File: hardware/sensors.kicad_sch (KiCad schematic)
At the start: 2 parts

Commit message: train schematics
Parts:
- added C? (x5): 0.1u, Capacitor_SMD:C_0603_1608Metric, symbol Device:C_Small
- added C? (x2): 4.7u, Capacitor_SMD:C_0805_2012Metric, symbol Device:C_Small
- added R? (x4): 4.7k, Resistor_SMD:R_0603_1608Metric, symbol Device:R_Small
- added R? (x5): 10k, Resistor_SMD:R_0603_1608Metric, symbol Device:R_Small
- U?: footprint (none) -> bt_Package_LGA:TE_MS563702BA03-50
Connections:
- net VDD_AUX_3V3: now reaches U?. (VDD)
- net VDD_AUX_3V3: now also U?.14 (VDD), C?.1, C?.1, C?.1, C?.1, R?.1, R?.1, R?.1, R?.1, R?.1, R?.1
- net at U?.1 (VDDIO): now also C?.1
- net at U?.10 (SA1/CS_B): now also R?.1, R?.2
- net IMU_INT1: now reaches U?.11 (INT1)
- net IMU_INT1: now also R?.2
- net GND: now reaches U?.12 (GND)
- net GND: now also U?.13 (RSVD), U?.3 (RSVD), U?.5 (GND), C?.2, C?.2, C?.2, C?.2, C?.2, R?.2, R?.2, R?.2
- net at U?.16 (RST): now also R?.1
- net at U?.2 (BYP): now also C?.1
- net SENSOR_I2C.SCL: now reaches U?.4 (SCL/SCLK)
- net SENSOR_I2C.SCL: now also U?. (VDD), R?.2
- net SENSOR_I2C.SDA: now reaches U?.6 (SDA/MOSI)
- net SENSOR_I2C.SDA: now also U?. (VDD), R?.2
- net at U?.7 (SA0/MISO): now also R?.1, R?.2
- net at U?.8 (CRST): now also C?.1
- net IMU_INT2: now reaches U?.9 (INT2)
- net IMU_INT2: now also R?.2
- new net: C?.2, C?.2, U?. (VDD)
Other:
- note added: "0xEC/0xED"
- note added: "SA1 SA0 I2C R/W ------------- 1 0 0x38/0x39 0 1 0x3A/0x3B 0 0 0x3C/0x3D 1 1 0x3E/0x3F"
- company: Erdapfel -> Frisius
- moved on the sheet: U?

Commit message: started b2b and power
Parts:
- removed R?: 4.7k, Resistor_SMD:R_0603_1608Metric, symbol Device:R_Small
- added TP?: IMU_ALERT, symbol Connector:TestPoint
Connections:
- net IMU_INT1: no longer names the net of R?.2, U?.11 (INT1)
- net IMU_INT1: now also TP?.1
- net IMU_INT2: no longer names the net of U?.9 (INT2)
- no-connect marks 0 -> 1
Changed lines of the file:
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@@
   (junction (at 43.18 82.55) (diameter 0) (color 0 0 0 0)
   )
-  (junction (at 119.38 27.94) (diameter 0) (color 0 0 0 0)
-  )
-  (junction (at 124.46 45.72) (diameter 0) (color 0 0 0 0)
+  (junction (at 119.38 41.91) (diameter 0) (color 0 0 0 0)
   )
   (junction (at 137.16 77.47) (diameter 0) (color 0 0 0 0)
@@
   (junction (at 78.74 36.83) (diameter 0) (color 0 0 0 0)
   )
-  (junction (at 119.38 43.18) (diameter 0) (color 0 0 0 0)
-  )
   (junction (at 114.3 27.94) (diameter 0) (color 0 0 0 0)
   )
@@
   (junction (at 43.18 36.83) (diameter 0) (color 0 0 0 0)
   )
+  (no_connect (at 96.52 76.2))
   (bus_entry (at 148.59 36.83) (size -2.54 2.54)
     (stroke (width 0) (type default) (color 0 0 0 0))
@@
     (stroke (width 0) (type default) (color 0 0 0 0))
   )
-  (wire (pts (xy 119.38 27.94) (xy 124.46 27.94))
-    (stroke (width 0) (type default) (color 0 0 0 0))
-  )
   (wire (pts (xy 134.62 76.2) (xy 134.62 77.47))
     (stroke (width 0) (type default) (color 0 0 0 0))
@@
     (stroke (width 0) (type default) (color 0 0 0 0))
   )
-  (wire (pts (xy 124.46 45.72) (xy 151.13 45.72))
-    (stroke (width 0) (type default) (color 0 0 0 0))
-  )
   (wire (pts (xy 109.22 26.67) (xy 109.22 27.94))
     (stroke (width 0) (type default) (color 0 0 0 0))
@@
     (stroke (width 0) (type default) (color 0 0 0 0))
   )
-  (wire (pts (xy 119.38 73.66) (xy 119.38 43.18))
+  (wire (pts (xy 119.38 34.29) (xy 119.38 41.91))
     (stroke (width 0) (type default) (color 0 0 0 0))
   )
@@
     (stroke (width 0) (type default) (color 0 0 0 0))
   )
-  (wire (pts (xy 119.38 43.18) (xy 151.13 43.18))
-    (stroke (width 0) (type default) (color 0 0 0 0))
-  )
   (bus (pts (xy 149.86 31.75) (xy 148.59 33.02))
     (stroke (width 0) (type default) (color 0 0 0 0))
@@
     (stroke (width 0) (type default) (color 0 0 0 0))
   )
-  (wire (pts (xy 119.38 34.29) (xy 119.38 43.18))
-    (stroke (width 0) (type default) (color 0 0 0 0))
-  )
   (wire (pts (xy 68.58 44.45) (xy 78.74 44.45))
     (stroke (width 0) (type default) (color 0 0 0 0))
@@
     (stroke (width 0) (type default) (color 0 0 0 0))
   )
-  (wire (pts (xy 96.52 76.2) (xy 124.46 76.2))
-    (stroke (width 0) (type default) (color 0 0 0 0))
-  )
   (wire (pts (xy 50.8 82.55) (xy 58.42 82.55))
     (stroke (width 0) (type default) (color 0 0 0 0))
   )
-  (wire (pts (xy 124.46 27.94) (xy 124.46 29.21))
-    (stroke (width 0) (type default) (color 0 0 0 0))
-  )
   (wire (pts (xy 58.42 64.77) (xy 58.42 69.85))
     (stroke (width 0) (type default) (color 0 0 0 0))
@@
     (stroke (width 0) (type default) (color 0 0 0 0))
   )
-  (wire (pts (xy 124.46 76.2) (xy 124.46 45.72))
-    (stroke (width 0) (type default) (color 0 0 0 0))
-  )
   (wire (pts (xy 96.52 82.55) (xy 97.79 82.55))
     (stroke (width 0) (type default) (color 0 0 0 0))
@@
     (stroke (width 0) (type default) (color 0 0 0 0))
   )
-  (wire (pts (xy 124.46 34.29) (xy 124.46 45.72))
+  (wire (pts (xy 119.38 41.91) (xy 119.38 73.66))
     (stroke (width 0) (type default) (color 0 0 0 0))
   )
@@
   )
   (hierarchical_label "SENSOR_I2C{SDA SCL}" (shape bidirectional) (at 151.13 31.75 0)
-    (effects (font (size 0.8 0.8)) (justify left))
-  )
-  (hierarchical_label "IMU_INT2" (shape bidirectional) (at 151.13 45.72 0)
-    (effects (font (size 0.8 0.8)) (justify left))
-  )
-  (hierarchical_label "IMU_INT1" (shape bidirectional) (at 151.13 43.18 0)
     (effects (font (size 0.8 0.8)) (justify left))
   )
@@
     (pin "1")
     (pin "2")
+  )
+  (symbol (lib_id "Connector:TestPoint") (at 119.38 41.91 270) (unit 1)
+    (in_bom yes) (on_board yes)
+    (property "Reference" "TP?" (id 0) (at 123.825 41.91 90)
+      (effects (font (size 0.8 0.8)) (justify left))
+    )
+    (property "Value" "IMU_ALERT" (id 1) (at 121.92 44.45 0)
+      (effects (font (size 0.8 0.8)) (justify left) hide)
+    )
+    (property "Footprint" "" (id 2) (at 119.38 46.99 0)
+      (effects (font (size 1.27 1.27)) hide)
+    )
+    (property "Datasheet" "~" (id 3) (at 119.38 46.99 0)
+      (effects (font (size 1.27 1.27)) hide)
+    )
+    (pin "1")
   )
   (symbol (lib_id "Device:R_Small") (at 119.38 31.75 0) (unit 1)
@@
     (pin "1")
   )
-  (symbol (lib_id "Device:R_Small") (at 124.46 31.75 0) (unit 1)
-    (in_bom yes) (on_board yes)
-    (property "Reference" "R?" (id 0) (at 125.73 30.48 0)
-      (effects (font (size 0.8 0.8)) (justify left))
-    )
-    (property "Value" "4.7k" (id 1) (at 125.73 31.75 0)
-      (effects (font (size 0.8 0.8)) (justify left))
-    )
-    (property "Footprint" "Resistor_SMD:R_0603_1608Metric" (id 2) (at 124.46 31.75 0)
-      (effects (font (size 0.8 0.8)) hide)
-    )
-    (property "Datasheet" "~" (id 3) (at 124.46 31.75 0)
-      (effects (font (size 0.8 0.8)) hide)
-    )
-    (pin "1")
-    (pin "2")
-  )
 )

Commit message: ready for first review
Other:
- moved on the sheet: C?, R?, TP?, U?

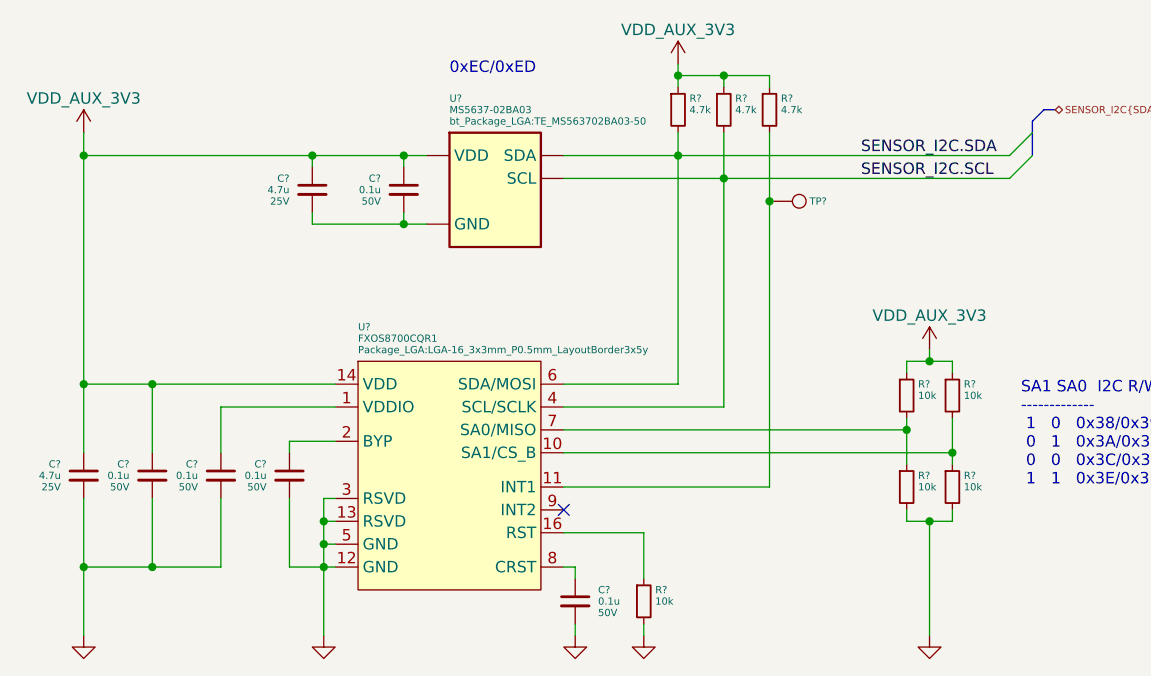
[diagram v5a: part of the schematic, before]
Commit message: checking footprint assignment, added current sense pac1934 for dev
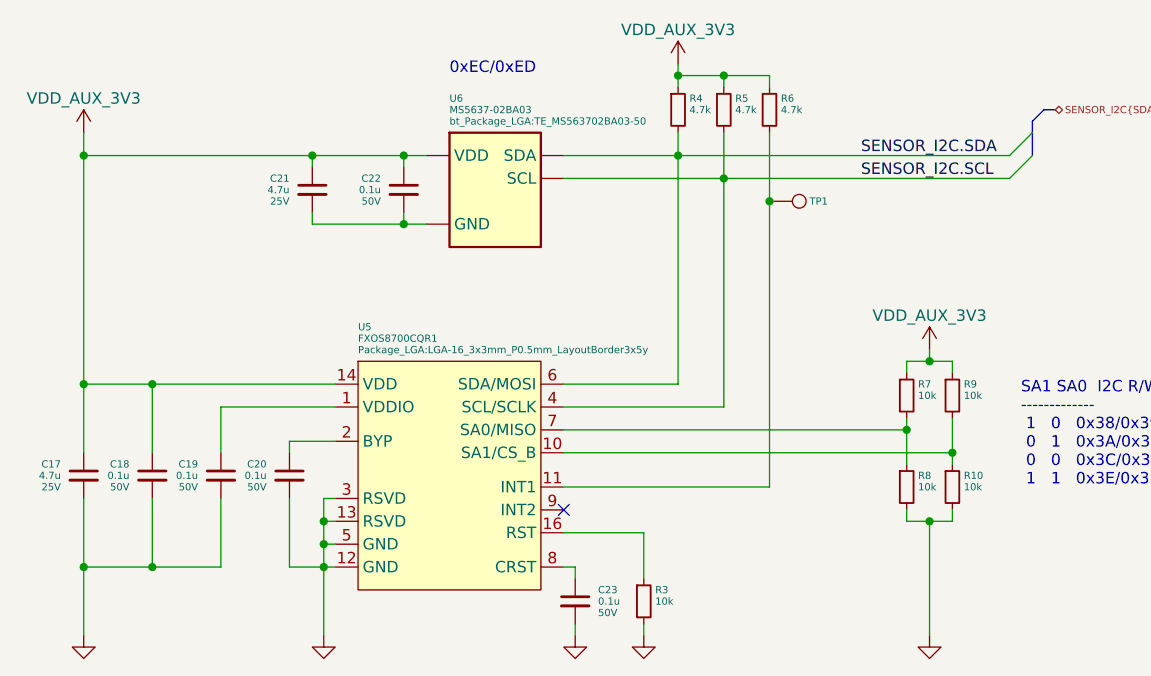
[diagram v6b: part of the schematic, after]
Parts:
- TP1: renamed from TP?; footprint (none) -> TestPoint:TestPoint_Pad_1.5x1.5mm
- gave numbers to parts that had none: 17
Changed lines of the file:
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@@
   (symbol (lib_id "Device:C_Small") (at 110.49 113.03 0) (mirror y) (unit 1)
     (in_bom yes) (on_board yes)
-    (property "Reference" "C?" (id 0) (at 107.95 111.76 0)
+    (property "Reference" "C19" (id 0) (at 107.95 111.76 0)
       (effects (font (size 0.8 0.8)) (justify left))
     )
@@
   (symbol (lib_id "Device:R_Small") (at 166.37 72.39 0) (unit 1)
     (in_bom yes) (on_board yes)
-    (property "Reference" "R?" (id 0) (at 167.64 71.12 0)
+    (property "Reference" "R5" (id 0) (at 167.64 71.12 0)
       (effects (font (size 0.8 0.8)) (justify left))
     )
@@
   (symbol (lib_id "Device:C_Small") (at 130.81 81.28 0) (mirror y) (unit 1)
     (in_bom yes) (on_board yes)
-    (property "Reference" "C?" (id 0) (at 128.27 80.01 0)
+    (property "Reference" "C22" (id 0) (at 128.27 80.01 0)
       (effects (font (size 0.8 0.8)) (justify left))
     )
@@
   (symbol (lib_id "bt_Sensor_Environmental:MS5637-02BA03") (at 140.97 80.01 0) (unit 1)
     (in_bom yes) (on_board yes)
-    (property "Reference" "U?" (id 0) (at 135.89 71.12 0)
+    (property "Reference" "U6" (id 0) (at 135.89 71.12 0)
       (effects (font (size 0.8 0.8)) (justify left))
     )
@@
   (symbol (lib_id "Device:C_Small") (at 118.11 113.03 0) (mirror y) (unit 1)
     (in_bom yes) (on_board yes)
-    (property "Reference" "C?" (id 0) (at 115.57 111.76 0)
+    (property "Reference" "C20" (id 0) (at 115.57 111.76 0)
       (effects (font (size 0.8 0.8)) (justify left))
     )
@@
   (symbol (lib_id "Device:C_Small") (at 149.86 127 0) (unit 1)
     (in_bom yes) (on_board yes)
-    (property "Reference" "C?" (id 0) (at 152.4 125.73 0)
+    (property "Reference" "C23" (id 0) (at 152.4 125.73 0)
       (effects (font (size 0.8 0.8)) (justify left))
     )
@@
   (symbol (lib_id "power:GND") (at 95.25 130.81 0) (unit 1)
     (in_bom yes) (on_board yes) (fields_autoplaced)
-    (property "Reference" "#PWR?" (id 0) (at 95.25 137.16 0)
+    (property "Reference" "#PWR016" (id 0) (at 95.25 137.16 0)
       (effects (font (size 1.27 1.27)) hide)
     )
@@
   (symbol (lib_id "Device:R_Small") (at 161.29 72.39 0) (unit 1)
     (in_bom yes) (on_board yes)
-    (property "Reference" "R?" (id 0) (at 162.56 71.12 0)
+    (property "Reference" "R4" (id 0) (at 162.56 71.12 0)
       (effects (font (size 0.8 0.8)) (justify left))
     )
@@
   (symbol (lib_id "Connector:TestPoint") (at 171.45 82.55 270) (unit 1)
     (in_bom yes) (on_board yes)
-    (property "Reference" "TP?" (id 0) (at 175.895 82.55 90)
+    (property "Reference" "TP1" (id 0) (at 175.895 82.55 90)
       (effects (font (size 0.8 0.8)) (justify left))
     )
@@
       (effects (font (size 0.8 0.8)) (justify left) hide)
     )
-    (property "Footprint" "" (id 2) (at 171.45 87.63 0)
+    (property "Footprint" "TestPoint:TestPoint_Pad_1.5x1.5mm" (id 2) (at 171.45 87.63 0)
       (effects (font (size 1.27 1.27)) hide)
     )
@@
   (symbol (lib_id "Device:R_Small") (at 171.45 72.39 0) (unit 1)
     (in_bom yes) (on_board yes)
-    (property "Reference" "R?" (id 0) (at 172.72 71.12 0)
+    (property "Reference" "R6" (id 0) (at 172.72 71.12 0)
       (effects (font (size 0.8 0.8)) (justify left))
     )
@@
   (symbol (lib_id "power:GND") (at 121.92 130.81 0) (unit 1)
     (in_bom yes) (on_board yes) (fields_autoplaced)
-    (property "Reference" "#PWR?" (id 0) (at 121.92 137.16 0)
+    (property "Reference" "#PWR017" (id 0) (at 121.92 137.16 0)
       (effects (font (size 1.27 1.27)) hide)
     )
@@
   (symbol (lib_id "bt_power:VDD_AUX_3V3") (at 189.23 99.06 0) (unit 1)
     (in_bom no) (on_board no)
-    (property "Reference" "U?" (id 0) (at 189.7634 99.06 0)
+    (property "Reference" "#U08" (id 0) (at 189.7634 99.06 0)
       (effects (font (size 1.27 1.27)) hide)
     )
@@
   (symbol (lib_id "power:GND") (at 149.86 130.81 0) (unit 1)
     (in_bom yes) (on_board yes) (fields_autoplaced)
-    (property "Reference" "#PWR?" (id 0) (at 149.86 137.16 0)
+    (property "Reference" "#PWR018" (id 0) (at 149.86 137.16 0)
       (effects (font (size 1.27 1.27)) hide)
     )
@@
   (symbol (lib_id "Device:C_Small") (at 120.65 81.28 0) (mirror y) (unit 1)
     (in_bom yes) (on_board yes)
-    (property "Reference" "C?" (id 0) (at 118.11 80.01 0)
+    (property "Reference" "C21" (id 0) (at 118.11 80.01 0)
       (effects (font (size 0.8 0.8)) (justify left))
     )
@@
   (symbol (lib_id "Device:R_Small") (at 186.69 114.3 0) (unit 1)
     (in_bom yes) (on_board yes)
-    (property "Reference" "R?" (id 0) (at 187.96 113.03 0)
+    (property "Reference" "R8" (id 0) (at 187.96 113.03 0)
       (effects (font (size 0.8 0.8)) (justify left))
     )
@@
   (symbol (lib_id "Device:R_Small") (at 191.77 104.14 0) (unit 1)
     (in_bom yes) (on_board yes)
-    (property "Reference" "R?" (id 0) (at 193.04 102.87 0)
+    (property "Reference" "R9" (id 0) (at 193.04 102.87 0)
       (effects (font (size 0.8 0.8)) (justify left))
     )
@@
   (symbol (lib_id "Device:C_Small") (at 95.25 113.03 0) (mirror y) (unit 1)
     (in_bom yes) (on_board yes)
-    (property "Reference" "C?" (id 0) (at 92.71 111.76 0)
+    (property "Reference" "C17" (id 0) (at 92.71 111.76 0)
       (effects (font (size 0.8 0.8)) (justify left))
     )
@@
   (symbol (lib_id "Device:R_Small") (at 191.77 114.3 0) (unit 1)
     (in_bom yes) (on_board yes)
-    (property "Reference" "R?" (id 0) (at 193.04 113.03 0)
+    (property "Reference" "R10" (id 0) (at 193.04 113.03 0)
       (effects (font (size 0.8 0.8)) (justify left))
     )
@@
   (symbol (lib_id "power:GND") (at 189.23 130.81 0) (unit 1)
     (in_bom yes) (on_board yes) (fields_autoplaced)
-    (property "Reference" "#PWR?" (id 0) (at 189.23 137.16 0)
+    (property "Reference" "#PWR020" (id 0) (at 189.23 137.16 0)
       (effects (font (size 1.27 1.27)) hide)
     )
@@
   (symbol (lib_id "Device:R_Small") (at 186.69 104.14 0) (unit 1)
     (in_bom yes) (on_board yes)
-    (property "Reference" "R?" (id 0) (at 187.96 102.87 0)
+    (property "Reference" "R7" (id 0) (at 187.96 102.87 0)
       (effects (font (size 0.8 0.8)) (justify left))
     )
@@
   (symbol (lib_id "bt_power:VDD_AUX_3V3") (at 95.25 74.93 0) (unit 1)
     (in_bom no) (on_board no)
-    (property "Reference" "U?" (id 0) (at 95.7834 74.93 0)
+    (property "Reference" "#U04" (id 0) (at 95.7834 74.93 0)
       (effects (font (size 1.27 1.27)) hide)
     )
@@
   (symbol (lib_id "bt_Sensor_Motion:FXOS8700CQR1") (at 135.89 113.03 0) (unit 1)
     (in_bom yes) (on_board yes)
-    (property "Reference" "U?" (id 0) (at 125.73 96.52 0)
+    (property "Reference" "U5" (id 0) (at 125.73 96.52 0)
       (effects (font (size 0.8 0.8)) (justify left))
     )
@@
   (symbol (lib_id "power:GND") (at 157.48 130.81 0) (unit 1)
     (in_bom yes) (on_board yes) (fields_autoplaced)
-    (property "Reference" "#PWR?" (id 0) (at 157.48 137.16 0)
+    (property "Reference" "#PWR019" (id 0) (at 157.48 137.16 0)
       (effects (font (size 1.27 1.27)) hide)
     )
@@
   (symbol (lib_id "Device:R_Small") (at 157.48 127 0) (unit 1)
     (in_bom yes) (on_board yes)
-    (property "Reference" "R?" (id 0) (at 158.75 125.73 0)
+    (property "Reference" "R3" (id 0) (at 158.75 125.73 0)
       (effects (font (size 0.8 0.8)) (justify left))
     )
@@
   (symbol (lib_id "Device:C_Small") (at 102.87 113.03 0) (mirror y) (unit 1)
     (in_bom yes) (on_board yes)
-    (property "Reference" "C?" (id 0) (at 100.33 111.76 0)
+    (property "Reference" "C18" (id 0) (at 100.33 111.76 0)
       (effects (font (size 0.8 0.8)) (justify left))
     )
@@
   (symbol (lib_id "bt_power:VDD_AUX_3V3") (at 161.29 67.31 0) (unit 1)
     (in_bom no) (on_board no)
-    (property "Reference" "U?" (id 0) (at 161.8234 67.31 0)
-      (effects (font (size 1.27 1.27)) hide)
-    )
+    (property "Reference" "#U07" (id 0) (at 161.8234 67.31 0)
+      (effects (font (size 1.27 1.27)) hide)
+    )

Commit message: hardware update
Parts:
- removed C21: 4.7u, Capacitor_SMD:C_0805_2012Metric, symbol Device:C_Small
- removed R10, R7, R8, R9: 10k, Resistor_SMD:R_0603_1608Metric, symbol Device:R_Small
- removed R6: 4.7k, Resistor_SMD:R_0603_1608Metric, symbol Device:R_Small
- removed TP1: IMU_ALERT, TestPoint:TestPoint_Pad_1.5x1.5mm, symbol Connector:TestPoint
- C11: renamed from C17; footprint Capacitor_SMD:C_0805_2012Metric -> Capacitor_SMD:C_0603_1608Metric
- C12: renamed from C18; footprint Capacitor_SMD:C_0603_1608Metric -> Capacitor_SMD:C_0402_1005Metric
- C13: renamed from C19; footprint Capacitor_SMD:C_0603_1608Metric -> Capacitor_SMD:C_0402_1005Metric
- C14: renamed from C20; footprint Capacitor_SMD:C_0603_1608Metric -> Capacitor_SMD:C_0402_1005Metric
- C15: renamed from C22; footprint Capacitor_SMD:C_0603_1608Metric -> Capacitor_SMD:C_0402_1005Metric
- C16: renamed from C23; footprint Capacitor_SMD:C_0603_1608Metric -> Capacitor_SMD:C_0402_1005Metric
- R2: renamed from R3; footprint Resistor_SMD:R_0603_1608Metric -> Resistor_SMD:R_0402_1005Metric
- R3: renamed from R4; footprint Resistor_SMD:R_0603_1608Metric -> Resistor_SMD:R_0402_1005Metric
- R4: renamed from R5; footprint Resistor_SMD:R_0603_1608Metric -> Resistor_SMD:R_0402_1005Metric
- renumbered U5 to U2, U6 to U3
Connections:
- net GND: now also U2.10 (SA1/CS_B), U2.7 (SA0/MISO)
- no-connect marks 1 -> 2

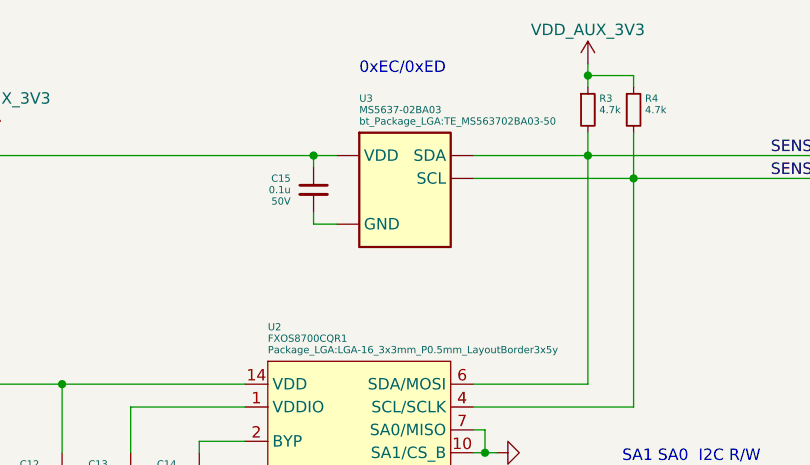
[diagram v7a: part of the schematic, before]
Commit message: initial component placement and design simplification
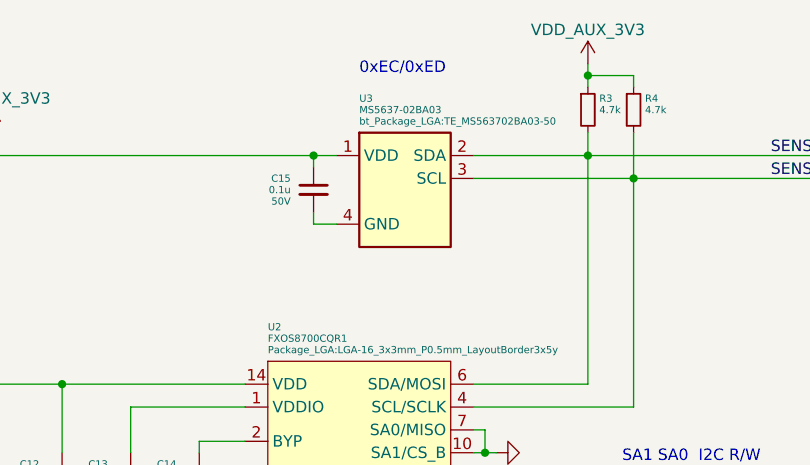
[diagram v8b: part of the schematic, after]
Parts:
- C11: footprint Capacitor_SMD:C_0603_1608Metric -> Capacitor_SMD:C_0402_1005Metric
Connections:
- net SENSOR_I2C.SCL: now also U3.3 (SCL); no longer U3. (VDD)
- net SENSOR_I2C.SDA: now also U3.2 (SDA); no longer U3. (VDD)
- net VDD_AUX_3V3: now also U3.1 (VDD); no longer U3. (VDD)
- net at C15.2: now also U3.4 (GND); no longer U3. (VDD)
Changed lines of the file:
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@@
       (effects (font (size 0.8 0.8)) hide)
     )
-    (pin "")
-    (pin "")
-    (pin "")
-    (pin "")
+    (pin "1")
+    (pin "2")
+    (pin "3")
+    (pin "4")
   )
   (symbol (lib_id "Device:C_Small") (at 118.11 113.03 0) (mirror y) (unit 1)
@@
       (effects (font (size 0.8 0.8)) (justify left))
     )
-    (property "Footprint" "Capacitor_SMD:C_0603_1608Metric" (id 2) (at 95.25 113.03 0)
+    (property "Footprint" "Capacitor_SMD:C_0402_1005Metric" (id 2) (at 95.25 113.03 0)
       (effects (font (size 0.8 0.8)) hide)
     )
